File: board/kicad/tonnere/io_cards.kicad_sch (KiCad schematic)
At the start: 11 parts, among them U39 TPD4E02B04DQA, U40 TPD4E02B04DQA

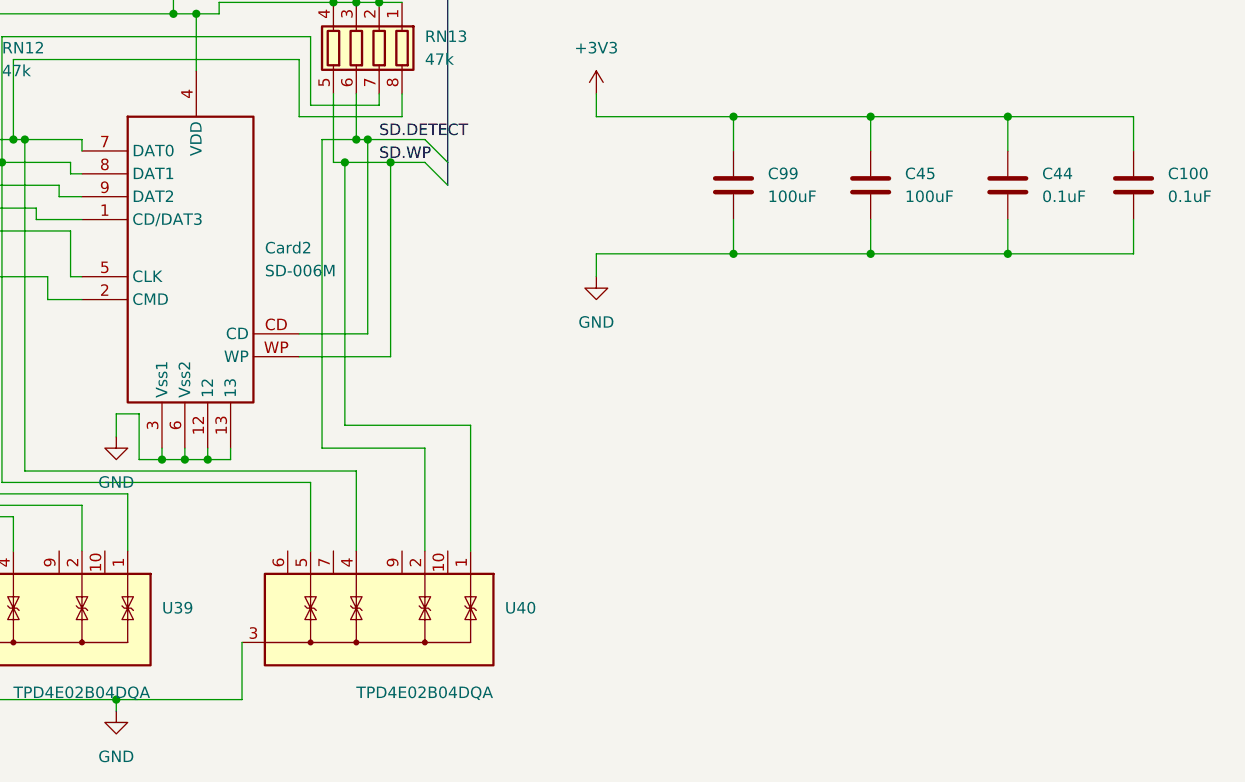
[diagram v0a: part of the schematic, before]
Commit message: 0.60 (not final). Fix errata from 0.51. Added USB2 phy.
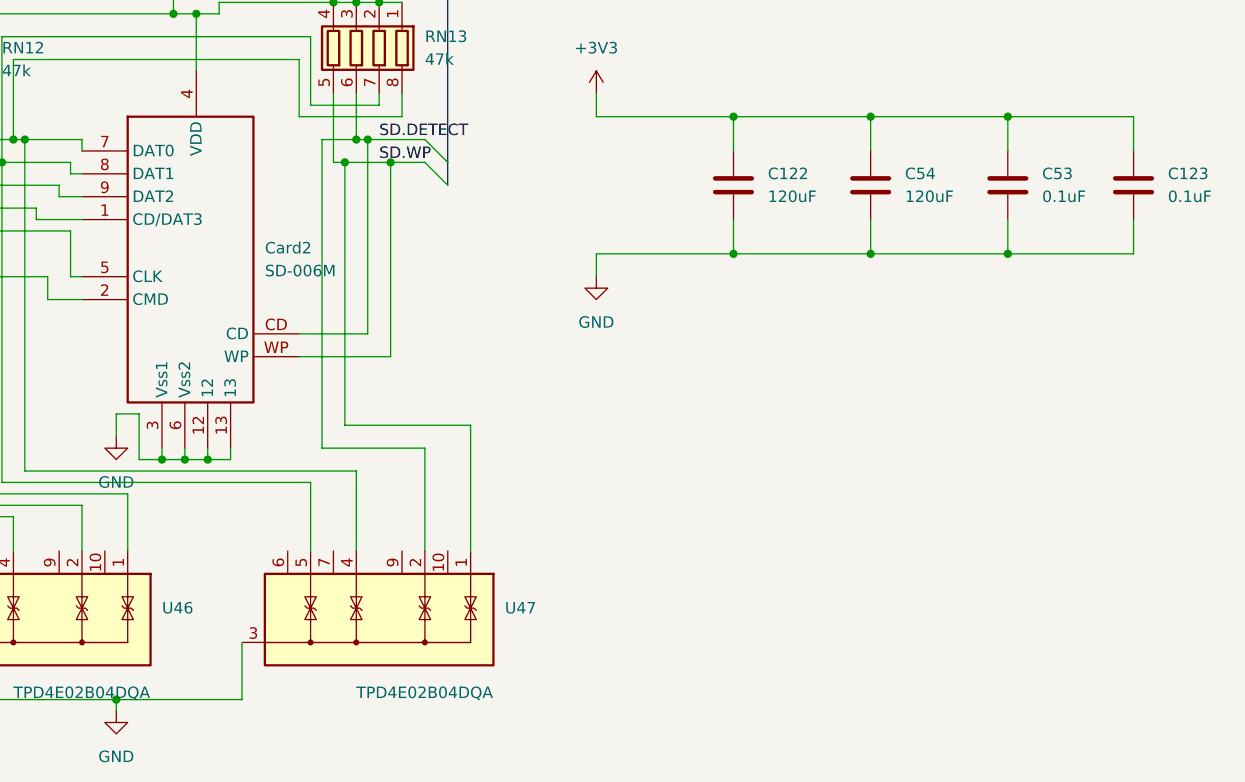
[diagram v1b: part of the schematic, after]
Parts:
- C122: renamed from C99; value 100uF -> 120uF
- C54: renamed from C45; value 100uF -> 120uF
- Card2: JLC_3DModel (none) -> 2b9048296755420789f7f276da73fcbc; JLC_3D_Size (none) -> 28.5 30
- renumbered C100 to C123, C44 to C53, U39 to U46, U40 to U47
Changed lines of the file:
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@@
 		(on_board yes)
 		(dnp no)
-		(property "Reference" "U40"
+		(property "Reference" "U47"
 			(at 172.72 83.8199 90)
 			(effects
@@
 			(project "tonnere"
 				(path "/eb8e239c-f2ec-4b57-8f5c-6c75d6b59ab3/6e470164-ad0d-4d1f-a1f3-2d1a639770a2"
-					(reference "U40")
+					(reference "U47")
 					(unit 1)
 				)
@@
 		(on_board yes)
 		(dnp no)
-		(property "Reference" "U39"
+		(property "Reference" "U46"
 			(at 134.62 83.8199 90)
 			(effects
@@
 			(project "tonnere"
 				(path "/eb8e239c-f2ec-4b57-8f5c-6c75d6b59ab3/6e470164-ad0d-4d1f-a1f3-2d1a639770a2"
-					(reference "U39")
+					(reference "U46")
 					(unit 1)
 				)
@@
 		(dnp no)
 		(fields_autoplaced yes)
-		(property "Reference" "C45"
+		(property "Reference" "C54"
 			(at 217.17 35.5599 0)
 			(effects
@@
 			)
 		)
-		(property "Value" "100uF"
+		(property "Value" "120uF"
 			(at 217.17 38.0999 0)
 			(effects
@@
 			(project "tonnere"
 				(path "/eb8e239c-f2ec-4b57-8f5c-6c75d6b59ab3/6e470164-ad0d-4d1f-a1f3-2d1a639770a2"
-					(reference "C45")
+					(reference "C54")
 					(unit 1)
 				)
@@
 			)
 		)
+		(property "JLC_3DModel" "2b9048296755420789f7f276da73fcbc"
+			(at 134.62 41.91 0)
+			(effects
+				(font
+					(size 1.27 1.27)
+				)
+				(hide yes)
+			)
+		)
+		(property "JLC_3D_Size" "28.5 30"
+			(at 134.62 41.91 0)
+			(effects
+				(font
+					(size 1.27 1.27)
+				)
+				(hide yes)
+			)
+		)
 		(pin "1"
 		)
@@
 		(dnp no)
 		(fields_autoplaced yes)
-		(property "Reference" "C99"
+		(property "Reference" "C122"
 			(at 201.93 35.5599 0)
 			(effects
@@
 			)
 		)
-		(property "Value" "100uF"
+		(property "Value" "120uF"
 			(at 201.93 38.0999 0)
 			(effects
@@
 			(project "tonnere"
 				(path "/eb8e239c-f2ec-4b57-8f5c-6c75d6b59ab3/6e470164-ad0d-4d1f-a1f3-2d1a639770a2"
-					(reference "C99")
+					(reference "C122")
 					(unit 1)
 				)
@@
 		(dnp no)
 		(fields_autoplaced yes)
-		(property "Reference" "C100"
+		(property "Reference" "C123"
 			(at 246.38 35.5599 0)
 			(effects
@@
 			(project "tonnere"
 				(path "/eb8e239c-f2ec-4b57-8f5c-6c75d6b59ab3/6e470164-ad0d-4d1f-a1f3-2d1a639770a2"
-					(reference "C100")
+					(reference "C123")
 					(unit 1)
 				)
@@
 		(dnp no)
 		(fields_autoplaced yes)
-		(property "Reference" "C44"
+		(property "Reference" "C53"
 			(at 232.41 35.5599 0)
 			(effects
@@
 			(project "tonnere"
 				(path "/eb8e239c-f2ec-4b57-8f5c-6c75d6b59ab3/6e470164-ad0d-4d1f-a1f3-2d1a639770a2"
-					(reference "C44")
-					(unit 1)
-				)
+					(reference "C53")
+					(unit 1)
+				)
